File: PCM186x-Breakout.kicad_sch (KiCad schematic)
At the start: 15 parts, among them J1 Conn_01x15, J2 Conn_01x15

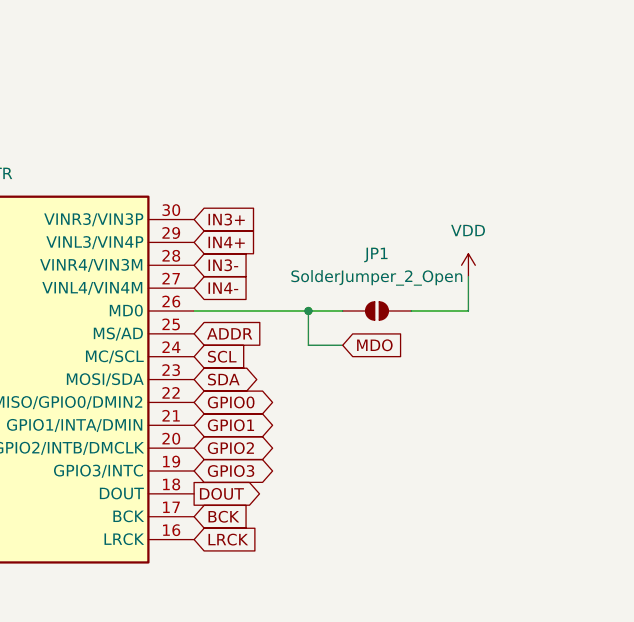
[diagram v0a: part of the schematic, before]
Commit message: addr pad, kicad 10, routing, silkscreen
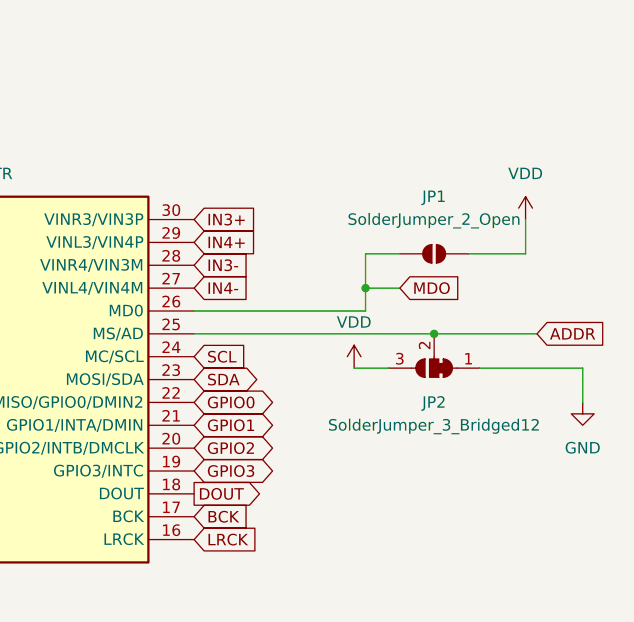
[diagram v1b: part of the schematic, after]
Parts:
- added JP2: SolderJumper_3_Bridged12, Jumper:SolderJumper-3_P1.3mm_Bridged12_RoundedPad1.0x1.5mm, symbol Jumper:SolderJumper_3_Bridged12
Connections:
- net ADDR: now also JP2.2 (C)
- net GND: now also JP2.1 (A)
- net VDD: now also JP2.3 (B)
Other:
- moved on the sheet: JP1

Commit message: make unused pins ground
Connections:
- net GND: now also J1.1 (Pin_1), J1.2 (Pin_2), J1.3 (Pin_3), J1.4 (Pin_4), J1.5 (Pin_5), J1.7 (Pin_7)
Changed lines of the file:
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@@
 	(paper "A4")
 	(junction
+		(at 209.55 50.8)
+		(diameter 0)
+		(color 0 0 0 0)
+	)
+	(junction
+		(at 212.09 50.8)
+		(diameter 0)
+		(color 0 0 0 0)
+	)
+	(junction
+		(at 204.47 50.8)
+		(diameter 0)
+		(color 0 0 0 0)
+	)
+	(junction
 		(at 156.21 115.57)
 		(diameter 0)
@@
 	)
 	(junction
+		(at 207.01 50.8)
+		(diameter 0)
+		(color 0 0 0 0)
+	)
+	(junction
 		(at 43.18 86.36)
 		(diameter 0)
@@
 	)
 	(junction
+		(at 214.63 50.8)
+		(diameter 0)
+		(color 0 0 0 0)
+	)
+	(junction
 		(at 260.35 97.79)
 		(diameter 0)
@@
 	(wire
 		(pts
+			(xy 209.55 50.8) (xy 207.01 50.8)
+		)
+		(stroke
+			(width 0)
+			(type default)
+		)
+	)
+	(wire
+		(pts
 			(xy 38.1 88.9) (xy 48.26 88.9)
 		)
@@
 	(wire
 		(pts
+			(xy 212.09 45.72) (xy 212.09 50.8)
+		)
+		(stroke
+			(width 0)
+			(type default)
+		)
+	)
+	(wire
+		(pts
+			(xy 204.47 45.72) (xy 204.47 50.8)
+		)
+		(stroke
+			(width 0)
+			(type default)
+		)
+	)
+	(wire
+		(pts
+			(xy 214.63 45.72) (xy 214.63 50.8)
+		)
+		(stroke
+			(width 0)
+			(type default)
+		)
+	)
+	(wire
+		(pts
 			(xy 252.73 88.9) (xy 252.73 92.71)
 		)
@@
 	(wire
 		(pts
+			(xy 204.47 50.8) (xy 196.85 50.8)
+		)
+		(stroke
+			(width 0)
+			(type default)
+		)
+	)
+	(wire
+		(pts
 			(xy 81.28 104.14) (xy 96.52 104.14)
 		)
@@
 	(wire
 		(pts
+			(xy 219.71 45.72) (xy 219.71 50.8)
+		)
+		(stroke
+			(width 0)
+			(type default)
+		)
+	)
+	(wire
+		(pts
 			(xy 182.88 142.24) (xy 193.04 142.24)
 		)
@@
 	(wire
 		(pts
+			(xy 219.71 50.8) (xy 214.63 50.8)
+		)
+		(stroke
+			(width 0)
+			(type default)
+		)
+	)
+	(wire
+		(pts
 			(xy 163.83 102.87) (xy 180.34 102.87)
 		)
@@
 	(wire
 		(pts
+			(xy 207.01 45.72) (xy 207.01 50.8)
+		)
+		(stroke
+			(width 0)
+			(type default)
+		)
+	)
+	(wire
+		(pts
 			(xy 81.28 88.9) (xy 96.52 88.9)
 		)
@@
 	(wire
 		(pts
+			(xy 212.09 50.8) (xy 209.55 50.8)
+		)
+		(stroke
+			(width 0)
+			(type default)
+		)
+	)
+	(wire
+		(pts
 			(xy 40.64 125.73) (xy 40.64 120.65)
 		)
@@
 	(wire
 		(pts
+			(xy 209.55 45.72) (xy 209.55 50.8)
+		)
+		(stroke
+			(width 0)
+			(type default)
+		)
+	)
+	(wire
+		(pts
+			(xy 214.63 50.8) (xy 212.09 50.8)
+		)
+		(stroke
+			(width 0)
+			(type default)
+		)
+	)
+	(wire
+		(pts
 			(xy 265.43 101.6) (xy 276.86 101.6)
 		)
@@
 	(wire
 		(pts
+			(xy 207.01 50.8) (xy 204.47 50.8)
+		)
+		(stroke
+			(width 0)
+			(type default)
+		)
+	)
+	(wire
+		(pts
 			(xy 252.73 92.71) (xy 252.73 95.25)
 		)
@@
 					(unit 1)
 				)
+			)
+		)
+	)
+	(symbol
+		(lib_id "power:GND")
+		(at 196.85 50.8 0)
+		(unit 1)
+		(body_style 1)
+		(exclude_from_sim no)
+		(in_bom yes)
+		(on_board yes)
+		(in_pos_files yes)
+		(dnp no)
+		(fields_autoplaced yes)
+		(property "Reference" "#PWR021"
+			(at 196.85 57.15 0)
+			(hide yes)
+			(show_name no)
+			(do_not_autoplace no)
+			(effects
+				(font
+					(size 1.27 1.27)
+				)
+			)
+		)
+		(property "Value" "GND"
+			(at 196.85 55.88 0)
+			(show_name no)
+			(do_not_autoplace no)
+			(effects
+				(font
+					(size 1.27 1.27)
+				)
+			)
+		)
+		(property "Footprint" ""
+			(at 196.85 50.8 0)
+			(hide yes)
+			(show_name no)
+			(do_not_autoplace no)
+			(effects
+				(font
+					(size 1.27 1.27)
+				)
+			)
+		)
+		(property "Datasheet" ""
+			(at 196.85 50.8 0)
+			(hide yes)
+			(show_name no)
+			(do_not_autoplace no)
+			(effects
+				(font
+					(size 1.27 1.27)
+				)
+			)
+		)
+		(property "Description" "Power symbol creates a global label with name \"GND\" , ground"
+			(at 196.85 50.8 0)
+			(hide yes)
+			(show_name no)
+			(do_not_autoplace no)
+			(effects
+				(font
+					(size 1.27 1.27)
+				)
+			)
+		)
+		(pin "1"
+		)
+		(instances
+			(project "PCM186x-Breakout"
+				(path "/1015398a-f8c2-41d4-a5c2-977acacea4f4"
+					(reference "#PWR021")
+					(unit 1)
+				)

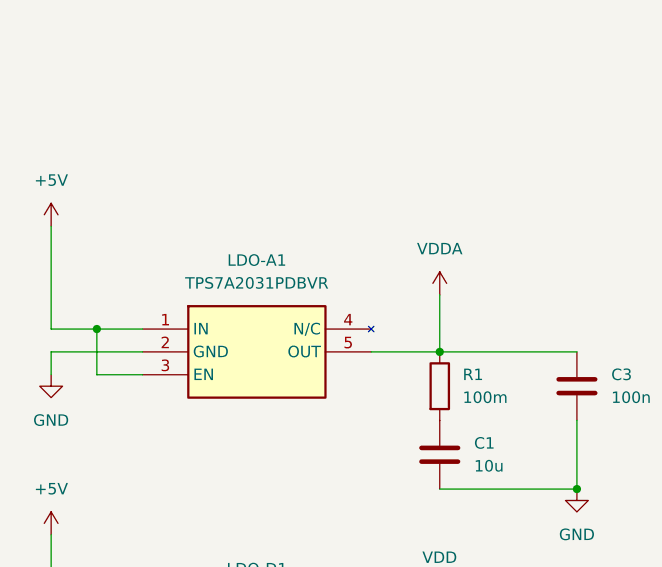
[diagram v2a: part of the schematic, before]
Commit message: specify 3.3 V version of analog LDO instead of 3.1 V version
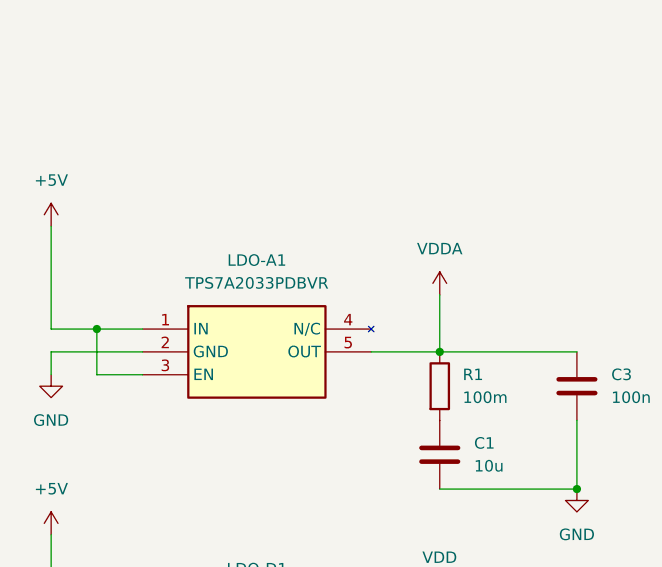
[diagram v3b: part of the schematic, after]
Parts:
- LDO-A1: value TPS7A2031PDBVR -> TPS7A2033PDBVR
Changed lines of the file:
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@@
 			)
 		)
-		(property "Value" "TPS7A2031PDBVR"
+		(property "Value" "TPS7A2033PDBVR"
 			(at 60.96 81.28 0)
 			(show_name no)
